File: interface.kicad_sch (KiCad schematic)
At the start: 5 parts, among them SW2 TS35CA

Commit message: save progress before refactor
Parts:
- added C26, C28: 10uF, Capacitor_SMD:C_0402_1005Metric, symbol Device:C_Small
- added C27: 1uF, Capacitor_SMD:C_0402_1005Metric, symbol Device:C_Small
- added C29: 2.2uF, Capacitor_SMD:C_0603_1608Metric, symbol Device:C_Small
- added C30: 4.7uF, Capacitor_SMD:C_0402_1005Metric, symbol Device:C_Small
- added C31: 15pF, Capacitor_SMD:C_0402_1005Metric, symbol Device:C_Small
- added C32: 4.7uF, Capacitor_SMD:C_0603_1608Metric, symbol Device:C_Small
- added D1: MBR0520, Diode_SMD:D_SOD-123, symbol Diode:MBR0520
- added J5: 5034801200, 5034801200:CON_5034801200_MOL, symbol 5034801200:5034801200
- added L4: 4.7uH, Inductor_SMD:L_1008_2520Metric, symbol Device:L_Small
- added R37: 100k, Resistor_SMD:R_0402_1005Metric, symbol Device:R_Small
- added R38: 560k, Resistor_SMD:R_0402_1005Metric, symbol Device:R_Small
- added R39: 820k, Resistor_SMD:R_0402_1005Metric, symbol Device:R_Small
- added R40: 130k, Resistor_SMD:R_0402_1005Metric, symbol Device:R_Small
- added U10: TPS61040DBV, Package_TO_SOT_SMD:SOT-23-5, symbol Regulator_Switching:TPS61040DBV
- added U9: AP3602AKTR-G1, AP3602AKTR-G1:SOT-23-6_L2.9-W1.6-P0.95-LS2.8-BR, symbol AP3602AKTR-G1:AP3602AKTR-G1
- C25: LCSC Part (none) -> C1525
- R11: LCSC Part (none) -> C25905
- R12: LCSC Part (none) -> C25744
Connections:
- net GND: now also LED1.2 (GND), C26.2, C28.2, C29.1, C30.2, C32.2, J5.11 (VSS), J5.4 (IM1), R37.2, R38.1, R40.2, U10.2 (GND), U9.2 (GND)
- net LED_DAT: now reaches LED1.3 (SDI)
- net LED_CLK: now reaches LED1.4 (CKL)
- net +5V: now reaches LED1.5 (VDD)
- net +5V: now also C28.1, U9.1 (VOUT)
- new net: C31.2, R39.2, R40.1, U10.3 (FB)
- new net: C27.2, U9.4 (C-)
- new net: C27.1, U9.6 (C+)
- new net: C29.2, J5.2 (VCOMH)
- new net: J5.5 (IREF), R38.2
- new net: D1.1 (K), L4.2, U10.1 (SW)
- new net +3V3_G1: J5.3 (VDD)
- new net +9V: C31.1, C32.1, D1.2 (A), J5.1 (VPP), R39.1
- new net LED_EN: R37.1, U9.3 (~{SHDN})
- new net OLED_CLK: J5.9 (D0)
- new net OLED_CS: J5.6 (CS#)
- new net OLED_DAT: J5.10 (D1)
- new net OLED_DC: J5.8 (A0)
- new net OLED_EN: U10.4 (EN)
- new net OLED_RST: J5.7 (RES#)
- new net VBAT: C26.1, C30.1, L4.1, U10.5 (VIN), U9.5 (VIN)
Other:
- note added: "Display: GY64128-03-C12"
- note added: "Isat>=500mA Low DCR"
- note added: "Must be >=16V"
- moved on the sheet: LED1

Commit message: progress dump
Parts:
- removed LED1: SK9822-EC20, SK9822-EC20:LED-SMD_6P-L2.0-W2.0-P0.80-TL, symbol SK9822-EC20:SK9822-EC20
- added LED1: XL-4020RGBC-WS2812B, XL-4020RGBC-2812B:LED-SMD_4P-L4.0-W1.7_XL-4020RGBC-WS2812B, symbol XL-4020RGBC-2812B:XL-4020RGBC-WS2812B
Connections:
- net +5V: now also LED1.1 (VSS)
- net GND: now also LED1.3 (VDD)
- net LED_DAT: now also LED1.4 (DI)
- no-connect marks 4 -> 3
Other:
- moved on the sheet: C30, C31, C32, D1, L4, R39, R40, U10

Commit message: finish up everything but nfc
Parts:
- added C39, C41, C42: 100nF, Capacitor_SMD:C_0402_1005Metric, symbol Device:C_Small
- added C40: 10uF, Capacitor_SMD:C_0402_1005Metric, symbol Device:C_Small
- added L6: JYLRA0832Z, custom_footprints:Generic_Solder_Pads_2P, symbol Device:L
- added U14: DRV2603RUNT, DRV2603RUNT:QFN-10_L2.0-W2.0-P0.50-TL, symbol DRV2603RUNT:DRV2603RUNT
- added U6: LIS2DW12TR, LIS2DW12TR:LGA-12_L2.0-W2.0-P0.50-BL, symbol LIS2DW12TR:LIS2DW12TR
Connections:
- net +3V3: now also C39.1, C40.1, C41.1, U14.1 (EN), U14.3 (LRA/~{ERM}), U6.10 (VDDIO), U6.9 (VDD)
- net GND: now also C39.2, C40.2, C41.2, C42.2, U14.10 (GND), U14.5 (GND), U14.8 (GND), U6.5 (NC), U6.6 (GND), U6.7 (RES), U6.8 (GND)
- net VBAT: now also C42.1, U14.7 (VDD)
- net +3V3_G1 renamed +3V3_G2
- new net ACC_INT: U6.12 (INT1)
- new net HAPTIC_PWM: U14.2 (PWM)
- new net LRA_OUTN: L6.2, U14.6 (OUT-)
- new net LRA_OUTP: L6.1, U14.9 (OUT+)
- new net SCL: U6.1 (SCL/SPC)
- new net SDA: U6.4 (SDA/SDI/SDO)
- no-connect marks 3 -> 7
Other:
- moved on the sheet: C29, J5, R38

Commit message: hopefully final schematic before splitting out
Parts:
- L5: renamed from L6; now left out of the parts list
- renumbered C42 to C26, C30 to C27, C29 to C28, C31 to C29, C32 to C30, C25 to C31, C26 to C32, C39 to C33, C40 to C34, C41 to C35, C27 to C36, C28 to C37, R38 to R14, R40 to R15, R39 to R16, R11 to R17, R12 to R18, R37 to R19, SW2 to SW1, U6 to U10, U9 to U11, U14 to U8, U10 to U9

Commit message: final review, fixes, cleanup
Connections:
- net +3V3: no longer U8.1 (EN)
- net +3V3_G2: now also J5.10 (VDD); no longer J5.3 (VDD)
- net +5V: now also LED1.3 (VDD); no longer LED1.1 (VSS)
- net +9V: now also J5.12 (VPP); no longer J5.1 (VPP)
- net GND: now also J5.2 (VSS), J5.9 (IM1), LED1.1 (VSS); no longer J5.11 (VSS), J5.4 (IM1), LED1.3 (VDD), U10.5 (NC)
- net OLED_CLK: now also J5.4 (D0); no longer J5.9 (D0)
- net OLED_CS: now also J5.7 (CS#); no longer J5.6 (CS#)
- net OLED_DAT: now also J5.3 (D1); no longer J5.10 (D1)
- net OLED_DC: now also J5.5 (A0); no longer J5.8 (A0)
- net OLED_RST: now also J5.6 (RES#); no longer J5.7 (RES#)
- net at C28.2: now also J5.11 (VCOMH); no longer J5.2 (VCOMH)
- net at R14.2: now also J5.8 (IREF); no longer J5.5 (IREF)
- new net HAPTIC_EN: U8.1 (EN)
- no-connect marks 7 -> 8
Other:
- note added: "Note: pins are mirrored, display is mounted with the cable facing right"
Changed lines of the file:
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@@
 	(text "Display: GY64128-03-C12"
 		(exclude_from_sim no)
-		(at 131.572 77.47 0)
+		(at 131.064 75.946 0)
 		(effects
 			(font
@@
 		)
 	)
+	(text "Note: pins are mirrored, display is\nmounted with the cable facing right"
+		(exclude_from_sim no)
+		(at 132.08 123.698 0)
+		(effects
+			(font
+				(size 1.27 1.27)
+			)
+		)
+	)
 	(text "Must be >=16V"
 		(exclude_from_sim no)
@@
 	)
 	(junction
-		(at 195.58 50.8)
-		(diameter 0)
-		(color 0 0 0 0)
-	)
-	(junction
 		(at 248.92 45.72)
 		(diameter 0)
@@
 	)
 	(no_connect
+		(at 198.12 48.26)
+	)
+	(no_connect
 		(at 194.31 90.17)
 	)
@@
 	(wire
 		(pts
-			(xy 195.58 48.26) (xy 198.12 48.26)
-		)
-		(stroke
-			(width 0)
-			(type default)
-		)
-	)
-	(wire
-		(pts
 			(xy 121.92 45.72) (xy 121.92 43.18)
 		)
@@
 	(wire
 		(pts
-			(xy 195.58 50.8) (xy 195.58 48.26)
-		)
-		(stroke
-			(width 0)
-			(type default)
-		)
-	)
-	(wire
-		(pts
 			(xy 257.81 121.92) (xy 269.24 121.92)
 		)
@@
 		)
 	)
+	(global_label "HAPTIC_EN"
+		(shape input)
+		(at 53.34 43.18 180)
+		(fields_autoplaced yes)
+		(effects
+			(font
+				(size 1.27 1.27)
+			)
+			(justify right)
+		)
+		(property "Intersheetrefs" "${INTERSHEET_REFS}"
+			(at 40.3762 43.18 0)
+			(effects
+				(font
+					(size 1.27 1.27)
+				)
+				(justify right)
+				(hide yes)
+			)
+		)
+	)
 	(global_label "SCL"
 		(shape input)
@@
 	(symbol
 		(lib_id "power:GND")
-		(at 238.76 154.94 270)
+		(at 238.76 149.86 270)
 		(unit 1)
 		(exclude_from_sim no)
@@
 		(dnp no)
 		(property "Reference" "#PWR092"
-			(at 232.41 154.94 0)
+			(at 232.41 149.86 0)
 			(effects
 				(font
@@
 		)
 		(property "Value" "GND"
-			(at 235.966 154.94 90)
+			(at 235.966 149.86 90)
 			(effects
 				(font
@@
 		)
 		(property "Footprint" ""
-			(at 238.76 154.94 0)
+			(at 238.76 149.86 0)
 			(effects
 				(font
@@
 		)
 		(property "Datasheet" ""
-			(at 238.76 154.94 0)
+			(at 238.76 149.86 0)
 			(effects
 				(font
@@
 		)
 		(property "Description" "Power symbol creates a global label with name \"GND\" , ground"
-			(at 238.76 154.94 0)
+			(at 238.76 149.86 0)
 			(effects
 				(font
@@
 	(symbol
 		(lib_id "power:+5V")
-		(at 238.76 149.86 90)
+		(at 238.76 154.94 90)
 		(unit 1)
 		(exclude_from_sim no)
@@
 		(dnp no)
 		(property "Reference" "#PWR091"
-			(at 242.57 149.86 0)
+			(at 242.57 154.94 0)
 			(effects
 				(font
@@
 		)
 		(property "Value" "+5V"
-			(at 235.966 149.86 90)
+			(at 235.966 154.94 90)
 			(effects
 				(font
@@
 		)
 		(property "Footprint" ""
-			(at 238.76 149.86 0)
+			(at 238.76 154.94 0)
 			(effects
 				(font
@@
 		)
 		(property "Datasheet" ""
-			(at 238.76 149.86 0)
+			(at 238.76 154.94 0)
 			(effects
 				(font
@@
 		)
 		(property "Description" "Power symbol creates a global label with name \"+5V\""
-			(at 238.76 149.86 0)
+			(at 238.76 154.94 0)
 			(effects
 				(font
@@
 					(unit 1)
 				)
-			)
-		)
-	)
-	(symbol
-		(lib_id "power:+3V3")
-		(at 53.34 43.18 90)
-		(unit 1)
-		(exclude_from_sim no)
-		(in_bom yes)
-		(on_board yes)
-		(dnp no)
-		(property "Reference" "#PWR066"
-			(at 57.15 43.18 0)
-			(effects
-				(font
-					(size 1.27 1.27)
-				)
-				(hide yes)
-			)
-		)
-		(property "Value" "+3V3"
-			(at 50.546 43.18 90)
-			(effects
-				(font
-					(size 1.27 1.27)
-				)
-				(justify left)
-			)
-		)
-		(property "Footprint" ""
-			(at 53.34 43.18 0)
-			(effects
-				(font
-					(size 1.27 1.27)
-				)
-				(hide yes)
-			)
-		)
-		(property "Datasheet" ""
-			(at 53.34 43.18 0)
-			(effects
-				(font
-					(size 1.27 1.27)
-				)
-				(hide yes)
-			)
-		)
-		(property "Description" "Power symbol creates a global label with name \"+3V3\""
-			(at 53.34 43.18 0)
-			(effects
-				(font
-					(size 1.27 1.27)
-				)
-				(hide yes)
-			)
-		)
-		(pin "1"
-		)
-		(instances
-			(project ""
-				(path "/c6cb5a1d-9f97-4766-8582-a9e93ed049e4/24c06676-89c1-498c-8350-9d02668ef39e"
-					(reference "#PWR066")
-					(unit 1)
-				)

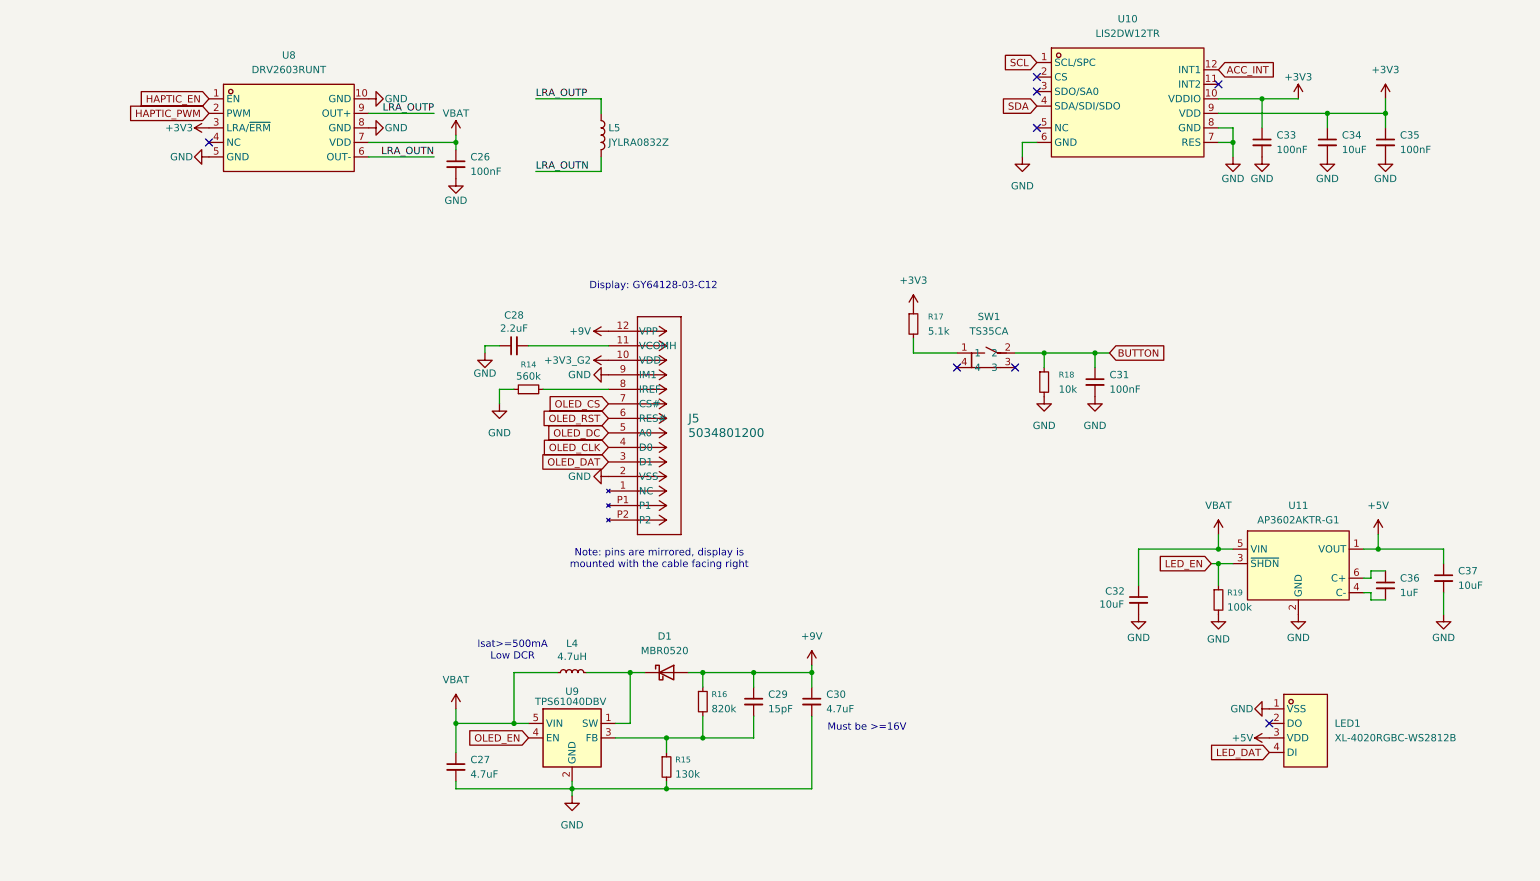
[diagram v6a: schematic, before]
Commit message: prepare schematic for devboard
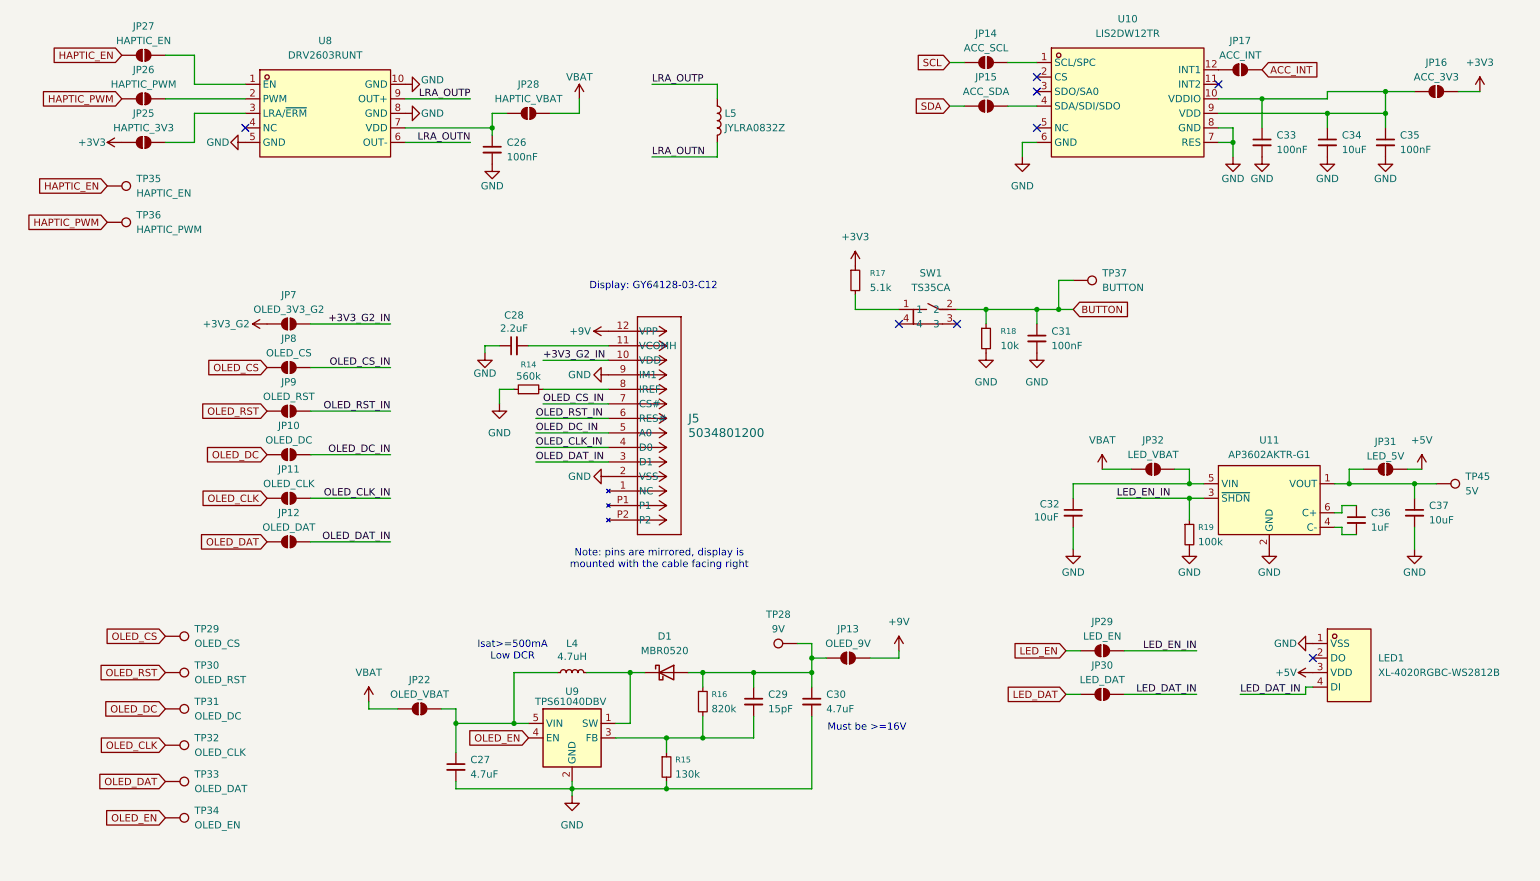
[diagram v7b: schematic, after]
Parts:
- added JP10: OLED_DC, Jumper:SolderJumper-2_P1.3mm_Open_Pad1.0x1.5mm, symbol Jumper:SolderJumper_2_Open
- added JP11: OLED_CLK, Jumper:SolderJumper-2_P1.3mm_Open_Pad1.0x1.5mm, symbol Jumper:SolderJumper_2_Open
- added JP12: OLED_DAT, Jumper:SolderJumper-2_P1.3mm_Open_Pad1.0x1.5mm, symbol Jumper:SolderJumper_2_Open
- added JP13: OLED_9V, Jumper:SolderJumper-2_P1.3mm_Open_Pad1.0x1.5mm, symbol Jumper:SolderJumper_2_Open
- added JP14: ACC_SCL, Jumper:SolderJumper-2_P1.3mm_Open_Pad1.0x1.5mm, symbol Jumper:SolderJumper_2_Open
- added JP15: ACC_SDA, Jumper:SolderJumper-2_P1.3mm_Open_Pad1.0x1.5mm, symbol Jumper:SolderJumper_2_Open
- added JP16: ACC_3V3, Jumper:SolderJumper-2_P1.3mm_Open_Pad1.0x1.5mm, symbol Jumper:SolderJumper_2_Open
- added JP17: ACC_INT, Jumper:SolderJumper-2_P1.3mm_Open_Pad1.0x1.5mm, symbol Jumper:SolderJumper_2_Open
- added JP22: OLED_VBAT, Jumper:SolderJumper-2_P1.3mm_Open_Pad1.0x1.5mm, symbol Jumper:SolderJumper_2_Open
- added JP25: HAPTIC_3V3, Jumper:SolderJumper-2_P1.3mm_Open_Pad1.0x1.5mm, symbol Jumper:SolderJumper_2_Open
- added JP26: HAPTIC_PWM, Jumper:SolderJumper-2_P1.3mm_Open_Pad1.0x1.5mm, symbol Jumper:SolderJumper_2_Open
- added JP27: HAPTIC_EN, Jumper:SolderJumper-2_P1.3mm_Open_Pad1.0x1.5mm, symbol Jumper:SolderJumper_2_Open
- added JP28: HAPTIC_VBAT, Jumper:SolderJumper-2_P1.3mm_Open_Pad1.0x1.5mm, symbol Jumper:SolderJumper_2_Open
- added JP29: LED_EN, Jumper:SolderJumper-2_P1.3mm_Open_Pad1.0x1.5mm, symbol Jumper:SolderJumper_2_Open
- added JP30: LED_DAT, Jumper:SolderJumper-2_P1.3mm_Open_Pad1.0x1.5mm, symbol Jumper:SolderJumper_2_Open
- added JP31: LED_5V, Jumper:SolderJumper-2_P1.3mm_Open_Pad1.0x1.5mm, symbol Jumper:SolderJumper_2_Open
- added JP32: LED_VBAT, Jumper:SolderJumper-2_P1.3mm_Open_Pad1.0x1.5mm, symbol Jumper:SolderJumper_2_Open
- added JP7: OLED_3V3_G2, Jumper:SolderJumper-2_P1.3mm_Open_Pad1.0x1.5mm, symbol Jumper:SolderJumper_2_Open
- added JP8: OLED_CS, Jumper:SolderJumper-2_P1.3mm_Open_Pad1.0x1.5mm, symbol Jumper:SolderJumper_2_Open
- added JP9: OLED_RST, Jumper:SolderJumper-2_P1.3mm_Open_Pad1.0x1.5mm, symbol Jumper:SolderJumper_2_Open
- added TP28: 9V, TestPoint:TestPoint_Pad_D1.0mm, symbol Connector:TestPoint
- added TP29: OLED_CS, TestPoint:TestPoint_Pad_D1.0mm, symbol Connector:TestPoint
- added TP30: OLED_RST, TestPoint:TestPoint_Pad_D1.0mm, symbol Connector:TestPoint
- added TP31: OLED_DC, TestPoint:TestPoint_Pad_D1.0mm, symbol Connector:TestPoint
- added TP32: OLED_CLK, TestPoint:TestPoint_Pad_D1.0mm, symbol Connector:TestPoint
- added TP33: OLED_DAT, TestPoint:TestPoint_Pad_D1.0mm, symbol Connector:TestPoint
- added TP34: OLED_EN, TestPoint:TestPoint_Pad_D1.0mm, symbol Connector:TestPoint
- added TP35: HAPTIC_EN, TestPoint:TestPoint_Pad_D1.0mm, symbol Connector:TestPoint
- added TP36: HAPTIC_PWM, TestPoint:TestPoint_Pad_D1.0mm, symbol Connector:TestPoint
- added TP37: BUTTON, TestPoint:TestPoint_Pad_D1.0mm, symbol Connector:TestPoint
- added TP45: 5V, TestPoint:TestPoint_Pad_D1.0mm, symbol Connector:TestPoint
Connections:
- net +3V3: now also JP16.2 (B), JP25.1 (A); no longer C33.1, C34.1, C35.1, U10.10 (VDDIO), U10.9 (VDD), U8.3 (LRA/~{ERM})
- net +3V3_G2: now also JP7.1 (A); no longer J5.10 (VDD)
- net +5V: now also JP31.2 (B); no longer C37.1, U11.1 (VOUT)
- net +9V: now also JP13.2 (B); no longer C29.1, C30.1, D1.2 (A), R16.1
- net ACC_INT: now also JP17.2 (B); no longer U10.12 (INT1)
- net BUTTON: now also TP37.1
- net HAPTIC_EN: now also JP27.1 (A), TP35.1; no longer U8.1 (EN)
- net HAPTIC_PWM: now also JP26.1 (A), TP36.1; no longer U8.2 (PWM)
- net LED_DAT: now also JP30.1 (A); no longer LED1.4 (DI)
- net LED_EN: now also JP29.1 (A); no longer R19.1, U11.3 (~{SHDN})
- net OLED_CLK: now also JP11.1 (A), TP32.1; no longer J5.4 (D0)
- net OLED_CS: now also JP8.1 (A), TP29.1; no longer J5.7 (CS#)
- net OLED_DAT: now also JP12.1 (A), TP33.1; no longer J5.3 (D1)
- net OLED_DC: now also JP10.1 (A), TP31.1; no longer J5.5 (A0)
- net OLED_EN: now also TP34.1
- net OLED_RST: now also JP9.1 (A), TP30.1; no longer J5.6 (RES#)
- net SCL: now also JP14.1 (A); no longer U10.1 (SCL/SPC)
- net SDA: now also JP15.1 (A); no longer U10.4 (SDA/SDI/SDO)
- net VBAT: now also JP22.1 (A), JP28.2 (B), JP32.1 (A); no longer C26.1, C27.1, C32.1, L4.1, U11.5 (VIN), U8.7 (VDD), U9.5 (VIN)
- new net: C29.1, C30.1, D1.2 (A), JP13.1 (A), R16.1, TP28.1
- new net: C37.1, JP31.1 (A), TP45.1, U11.1 (VOUT)
- new net: C32.1, JP32.2 (B), U11.5 (VIN)
- new net: JP27.2 (B), U8.1 (EN)
- new net: JP26.2 (B), U8.2 (PWM)
- new net: JP25.2 (B), U8.3 (LRA/~{ERM})
- new net: C26.1, JP28.1 (A), U8.7 (VDD)
- new net: JP17.1 (A), U10.12 (INT1)
- new net: JP15.2 (B), U10.4 (SDA/SDI/SDO)
- new net: C33.1, C34.1, C35.1, JP16.1 (A), U10.10 (VDDIO), U10.9 (VDD)
- new net: JP14.2 (B), U10.1 (SCL/SPC)
- new net: C27.1, JP22.2 (B), L4.1, U9.5 (VIN)
- new net +3V3_G2_IN: J5.10 (VDD), JP7.2 (B)
- new net LED_DAT_IN: JP30.2 (B), LED1.4 (DI)
- new net LED_EN_IN: JP29.2 (B), R19.1, U11.3 (~{SHDN})
- new net OLED_CLK_IN: J5.4 (D0), JP11.2 (B)
- new net OLED_CS_IN: J5.7 (CS#), JP8.2 (B)
- new net OLED_DAT_IN: J5.3 (D1), JP12.2 (B)
- new net OLED_DC_IN: J5.5 (A0), JP10.2 (B)
- new net OLED_RST_IN: J5.6 (RES#), JP9.2 (B)
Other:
- moved on the sheet: C26, C31, C32, C36, C37, L5, LED1, R17, R18, R19, SW1, U11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

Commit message: huge progress on bentoboard, schematic fixes
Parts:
- removed JP25: HAPTIC_3V3, Jumper:SolderJumper-2_P1.3mm_Open_Pad1.0x1.5mm, symbol Jumper:SolderJumper_2_Open
- added JP43: OLED_EN, Jumper:SolderJumper-2_P1.3mm_Open_Pad1.0x1.5mm, symbol Jumper:SolderJumper_2_Open
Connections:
- net OLED_EN: now also JP43.1 (A); no longer U9.4 (EN)
- net HAPTIC_VBAT_IN: now reaches U8.3 (LRA/~{ERM})
- net HAPTIC_VBAT_IN: now also C26.1, JP28.1 (A), U8.7 (VDD)
- net ACC_3V3_IN: now reaches C33.1, C34.1, C35.1, JP16.1 (A), U10.10 (VDDIO), U10.9 (VDD)
- new net OLED_EN_IN: JP43.2 (B), U9.4 (EN)
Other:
- moved on the sheet: C26, JP16, JP28
